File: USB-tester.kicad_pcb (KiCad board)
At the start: 2 copper layers, 68.7 x 41.2 mm, 57 parts

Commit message: Version 2
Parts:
- removed USBC1, USBC2: 105450-0101, USB-C-SMD_TYPE-C-USB-18:USB-C-SMD_TYPE-C-USB-18
- added BAT1: S2B-ZR-SM4A-TF_LF__SN_, S2B-ZR-SM4A-TF_LF__SN_:JST_S2B-ZR-SM4A-TF_LF__SN_, B.Cu at (166.4, 116.1)
- added C1: 10uF, Capacitor_SMD:C_0603_1608Metric, B.Cu at (164.5, 100.5)
- added C2: 10uF, Capacitor_SMD:C_0603_1608Metric, B.Cu at (171.0, 100.4)
- added D1: RED, LED_SMD:LED_0603_1608Metric, F.Cu at (136.1, 110.7)
- added D2: GREEN, LED_SMD:LED_0603_1608Metric, F.Cu at (136.1, 108.9)
- added J1: TYPE-C-31-M-12, TYPE-C-31-M-12:HRO_TYPE-C-31-M-12, B.Cu at (146.9, 121.3)
- added R26: 220R, Resistor_SMD:R_0603_1608Metric, F.Cu at (139.5, 110.7)
- added R27: 5.1K, Resistor_SMD:R_0603_1608Metric, B.Cu at (163.7, 102.8)
- added R28: 220R, Resistor_SMD:R_0603_1608Metric, F.Cu at (139.5, 108.9)
- added R29: 5.1K, Resistor_SMD:R_0603_1608Metric, B.Cu at (153.6, 115.4)
- added R30: 5.1K, Resistor_SMD:R_0603_1608Metric, B.Cu at (153.6, 118.0)
- added U1: TP4057, Package_TO_SOT_SMD:SOT-23-6, B.Cu at (167.7, 100.3)
- added USB1: TYPEC-324-BCP24, easyeda2kicad:USB-C-SMD_TYPEC-324-BCP24, F.Cu at (196.2, 101.5)
- added USB2: TYPEC-324-BCP24, easyeda2kicad:USB-C-SMD_TYPEC-324-BCP24, F.Cu at (136.8, 100.7)
- moved D25 64.3 mm to (198.2, 91.3), turned to 180 degrees
- moved R25 63.4 mm to (198.2, 93.3), turned to 0 degrees
- turned BT2 to 0 degrees
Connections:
- net Net-(A1-K) renamed BAT-
- BT2 pad 1: A10_A -> A10_B
- R1 pad 2: B1_A -> B12_A
- R10 pad 2: B10_A -> B3_A
- R11 pad 2: B11_A -> B2_A
- R12 pad 2: B12_A -> B1_A
- R13 pad 2: A1_B -> A12_A
- R14 pad 2: A2_B -> A11_A
- R15 pad 2: A3_B -> A10_A
- R16 pad 2: A4_B -> A9_A
- R17 pad 2: A5_B -> A8_A
- R18 pad 2: A6_B -> A7_A
- R19 pad 2: A7_B -> A6_A
- R2 pad 2: B2_A -> B11_A
- R20 pad 2: A8_B -> A5_A
- R21 pad 2: A9_B -> A4_A
- R22 pad 2: A10_B -> A3_A
- R23 pad 2: A11_B -> A2_A
- R24 pad 2: A12_B -> A1_A
- R3 pad 2: B3_A -> B10_A
- R4 pad 2: B4_A -> B9_A
- R5 pad 2: B5_A -> B8_A
- R6 pad 2: B6_A -> B7_A
- R7 pad 2: B7_A -> B6_A
- R8 pad 2: B8_A -> B5_A
- R9 pad 2: B9_A -> B4_A
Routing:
- net BAT-: track 96.6 -> 206.7 mm, vias 1 -> 5
- net +5V: track 0.00 -> 63.0 mm, vias 0 -> 4
- net A10_B: track 22.8 -> 85.6 mm, vias 2 -> 3
- net Net-(D2-K): track 0.00 -> 50.2 mm, vias 0 -> 3
- net B5_A: track 15.3 -> 65.2 mm, vias 2 -> 6
- net B11_A: track 17.8 -> 66.6 mm
- net B12_A: track 16.6 -> 64.8 mm, vias 0 -> 1
- net B3_A: track 17.1 -> 65.0 mm
- net B2_A: track 18.6 -> 64.5 mm
- net B10_A: track 19.6 -> 65.1 mm, vias 2 -> 4
- net B1_A: track 17.7 -> 62.1 mm, vias 0 -> 1
- net B8_A: track 22.0 -> 65.4 mm, vias 2 -> 6
- net B4_A: track 14.8 -> 54.3 mm, vias 2 -> 1
- net Net-(D1-K): track 0.00 -> 39.4 mm, vias 0 -> 3
- net B6_A: track 14.4 -> 53.3 mm, vias 2 -> 1
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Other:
- board text added: "+"
- board text added: "-"
- board text added: "CHRG"
- board text added: "STDBY"
- board text added: "USB Tester Version 2.0"
- board text removed: "USB Tester Version 1.0"

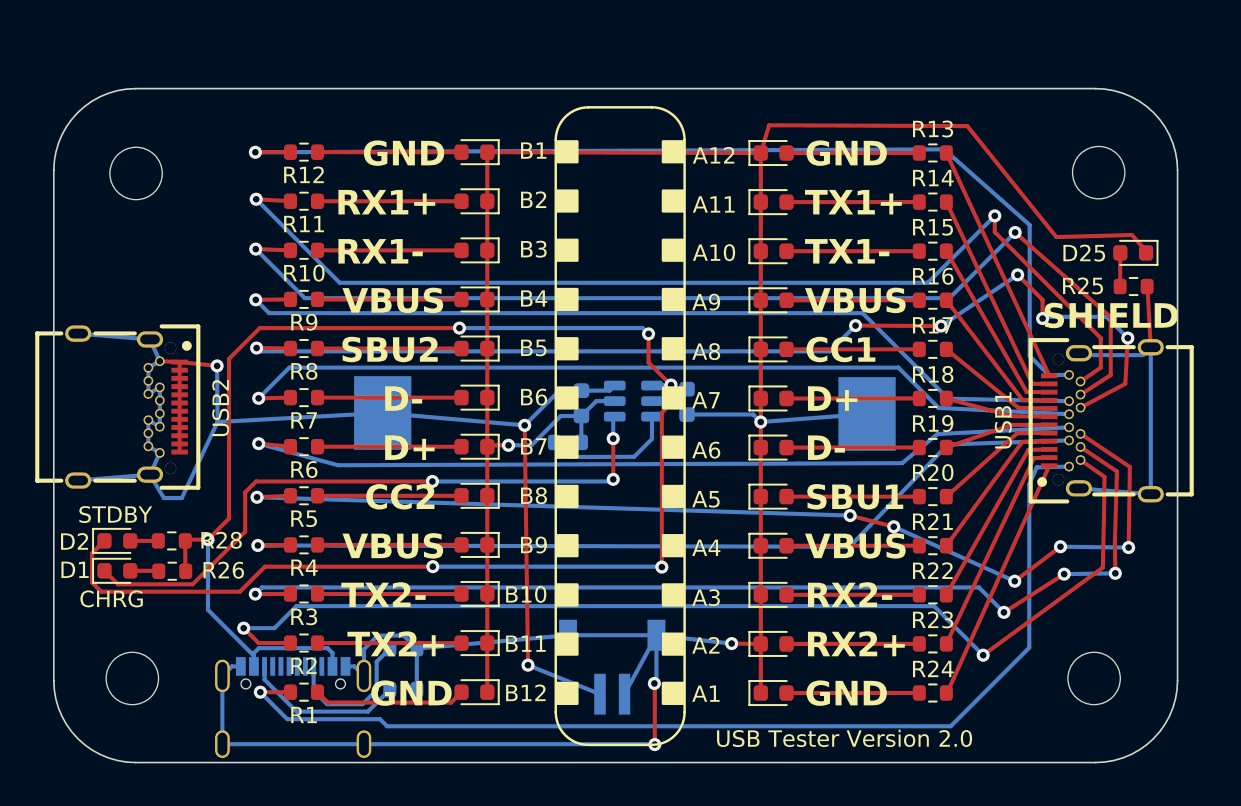
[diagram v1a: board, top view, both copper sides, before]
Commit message: Adds test points
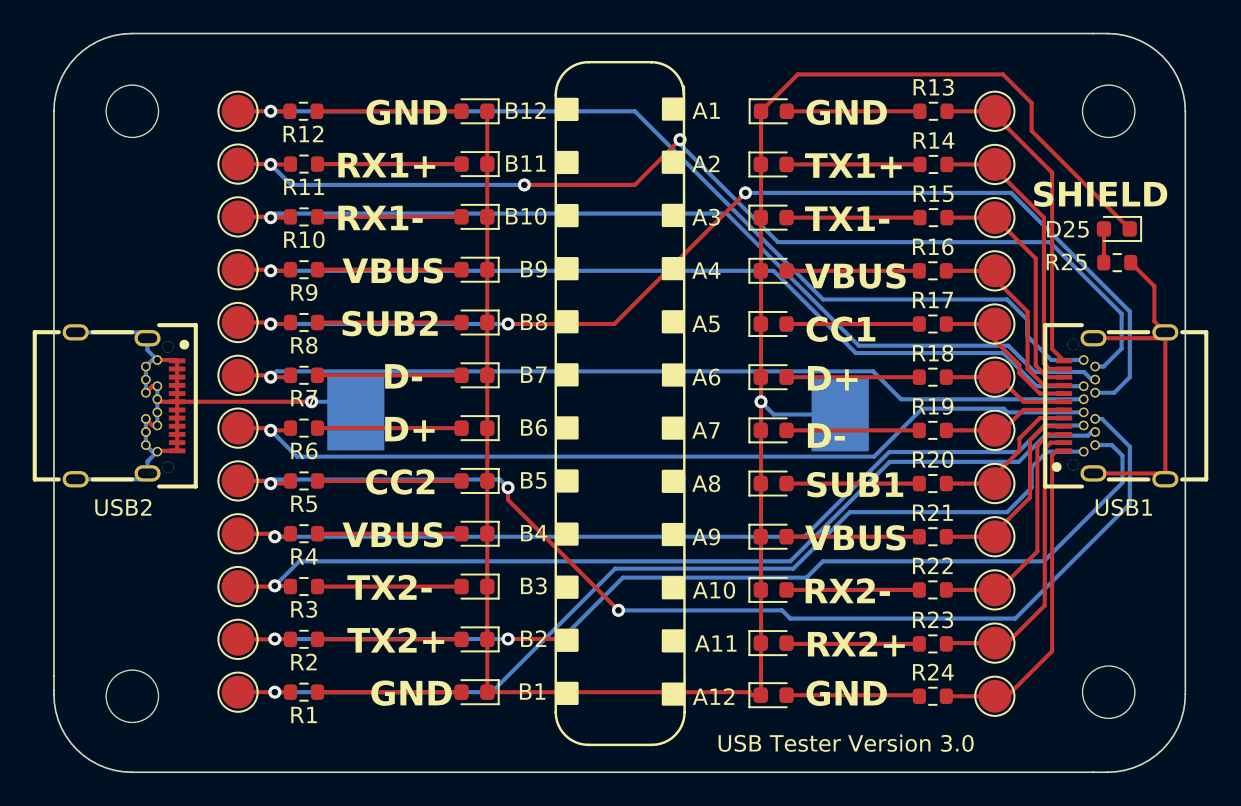
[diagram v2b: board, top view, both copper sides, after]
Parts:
- removed BAT1: S2B-ZR-SM4A-TF_LF__SN_, S2B-ZR-SM4A-TF_LF__SN_:JST_S2B-ZR-SM4A-TF_LF__SN_
- removed C1, C2: 10uF, Capacitor_SMD:C_0603_1608Metric
- removed D1: RED, LED_SMD:LED_0603_1608Metric
- removed D2: GREEN, LED_SMD:LED_0603_1608Metric
- removed J1: TYPE-C-31-M-12, TYPE-C-31-M-12:HRO_TYPE-C-31-M-12
- removed R26, R28: 220R, Resistor_SMD:R_0603_1608Metric
- removed R27, R29, R30: 5.1K, Resistor_SMD:R_0603_1608Metric
- removed U1: TP4057, Package_TO_SOT_SMD:SOT-23-6
- added TP1: GND, TestPoint:TestPoint_Pad_D2.0mm, F.Cu at (189.8, 118.4)
- added TP10: D-, TestPoint:TestPoint_Pad_D2.0mm, F.Cu at (189.8, 98.9)
- added TP11: SUB1, TestPoint:TestPoint_Pad_D2.0mm, F.Cu at (189.8, 95.6)
- added TP12: VBUS, TestPoint:TestPoint_Pad_D2.0mm, F.Cu at (189.8, 92.4)
- added TP13: RX-, TestPoint:TestPoint_Pad_D2.0mm, F.Cu at (189.8, 89.1)
- added TP14: GND, TestPoint:TestPoint_Pad_D2.0mm, F.Cu at (189.8, 82.6)
- added TP15: TX-, TestPoint:TestPoint_Pad_D2.0mm, F.Cu at (143.5, 89.1)
- added TP16: VBUS, TestPoint:TestPoint_Pad_D2.0mm, F.Cu at (143.5, 92.3)
- added TP17: CC2, TestPoint:TestPoint_Pad_D2.0mm, F.Cu at (143.5, 95.5)
- added TP18: D+, TestPoint:TestPoint_Pad_D2.0mm, F.Cu at (143.5, 98.7)
- added TP19: D-, TestPoint:TestPoint_Pad_D2.0mm, F.Cu at (143.5, 102.0)
- added TP2: D+, TestPoint:TestPoint_Pad_D2.0mm, F.Cu at (189.8, 102.1)
- added TP20: SUB2, TestPoint:TestPoint_Pad_D2.0mm, F.Cu at (143.5, 105.2)
- added TP21: VBUS, TestPoint:TestPoint_Pad_D2.0mm, F.Cu at (143.5, 108.4)
- added TP22: RX-, TestPoint:TestPoint_Pad_D2.0mm, F.Cu at (143.5, 111.7)
- added TP23: RX+, TestPoint:TestPoint_Pad_D2.0mm, F.Cu at (143.5, 114.9)
- added TP24: GND, TestPoint:TestPoint_Pad_D2.0mm, F.Cu at (143.5, 118.1)
- added TP3: RX+, TestPoint:TestPoint_Pad_D2.0mm, F.Cu at (189.8, 85.9)
- added TP4: GND, TestPoint:TestPoint_Pad_D2.0mm, F.Cu at (143.5, 82.6)
- added TP5: TX+, TestPoint:TestPoint_Pad_D2.0mm, F.Cu at (143.5, 85.8)
- added TP6: TX+, TestPoint:TestPoint_Pad_D2.0mm, F.Cu at (189.8, 115.1)
- added TP7: TX-, TestPoint:TestPoint_Pad_D2.0mm, F.Cu at (189.8, 111.9)
- added TP8: VBUS, TestPoint:TestPoint_Pad_D2.0mm, F.Cu at (189.8, 108.6)
- added TP9: CC1, TestPoint:TestPoint_Pad_D2.0mm, F.Cu at (189.8, 105.4)
- moved H1 3.81 mm to (137.1, 82.6)
- moved H3 3.80 mm to (196.7, 82.6)
- moved A1 2.55 mm to (176.3, 82.6)
- moved R13 2.55 mm to (186.0, 82.6)
- moved B12 2.50 mm to (158.0, 82.6)
- moved R12 2.50 mm to (147.5, 82.6)
- moved A2 2.30 mm to (176.3, 85.9)
- moved R14 2.30 mm to (186.0, 85.9)
- moved B11 2.27 mm to (158.0, 85.8)
- moved R11 2.27 mm to (147.5, 85.8)
- moved A3 2.05 mm to (176.3, 89.1)
- moved R15 2.05 mm to (186.0, 89.1)
- moved B10 2.05 mm to (158.0, 89.1)
- moved R10 2.04 mm to (147.5, 89.1)
- moved B9 1.82 mm to (158.0, 92.3)
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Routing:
- net BAT-: track 206.7 -> 121.5 mm, vias 5 -> 1
- net +5V: track 63.0 -> 0.00 mm, vias 4 -> 0
- net Net-(D2-K): track 50.2 -> 0.00 mm, vias 3 -> 0
- net A10_B: track 85.6 -> 41.7 mm, vias 3 -> 1
- net Net-(D1-K): track 39.4 -> 0.00 mm, vias 3 -> 0
- net Net-(J1-CC2): track 9.83 -> 0.00 mm
- net Net-(J1-CC1): track 8.90 -> 0.00 mm
- net Net-(U1-PROG): track 8.15 -> 0.00 mm
- net B10_A: track 65.1 -> 57.3 mm, vias 4 -> 1
- net B3_A: track 65.0 -> 58.0 mm, vias 2 -> 1
- net B8_A: track 65.4 -> 71.2 mm, vias 6 -> 3
- net B12_A: track 64.8 -> 59.5 mm
- net A12_A: track 15.0 -> 19.8 mm
- net A1_A: track 15.2 -> 20.0 mm
- net A2_A: track 13.5 -> 17.9 mm
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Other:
- board size 68.7 x 41.2 mm -> 69.1 x 45.1 mm
- board text added: "SUB1"
- board text added: "SUB2"
- board text added: "USB Tester Version 3.0"
- board text removed: "CHRG"
- board text removed: "SBU1"
- board text removed: "SBU2"
- board text removed: "STDBY"
- board text removed: "USB Tester Version 2.0"

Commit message: Break out version
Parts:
- removed TP1, TP14, TP24, TP4: GND, TestPoint:TestPoint_Pad_D2.0mm
- removed TP10, TP19: D-, TestPoint:TestPoint_Pad_D2.0mm
- removed TP11: SUB1, TestPoint:TestPoint_Pad_D2.0mm
- removed TP12, TP16, TP21, TP8: VBUS, TestPoint:TestPoint_Pad_D2.0mm
- removed TP13, TP22: RX-, TestPoint:TestPoint_Pad_D2.0mm
- removed TP15, TP7: TX-, TestPoint:TestPoint_Pad_D2.0mm
- removed TP17: CC2, TestPoint:TestPoint_Pad_D2.0mm
- removed TP18, TP2: D+, TestPoint:TestPoint_Pad_D2.0mm
- removed TP20: SUB2, TestPoint:TestPoint_Pad_D2.0mm
- removed TP23, TP3: RX+, TestPoint:TestPoint_Pad_D2.0mm
- removed TP5, TP6: TX+, TestPoint:TestPoint_Pad_D2.0mm
- removed TP9: CC1, TestPoint:TestPoint_Pad_D2.0mm
- added J1: Conn_02x12_Odd_Even, Connector_PinSocket_2.54mm:PinSocket_2x12_P2.54mm_Vertical, F.Cu at (165.5, 114.2)
- added J2: Conn_01x02, Connector_PinSocket_2.54mm:PinSocket_1x02_P2.54mm_Vertical, F.Cu at (136.5, 92.1)
- moved BT2 14.5 mm to (151.0, 100.1), turned to 90 degrees
- moved R24 4.04 mm to (186.0, 114.3)
- moved A12 3.93 mm to (176.3, 114.4)
- moved R1 3.79 mm to (147.5, 114.3)
- moved B1 3.75 mm to (158.0, 114.4)
- moved B12 3.54 mm to (158.0, 86.1)
- moved A1 3.54 mm to (176.3, 86.1)
- moved R12 3.50 mm to (147.5, 86.1)
- moved R13 3.50 mm to (186.0, 86.1)
- moved R23 3.40 mm to (186.0, 111.8)
- moved A11 3.32 mm to (176.3, 111.8)
- moved R2 3.13 mm to (147.5, 111.8)
- moved B2 3.09 mm to (158.0, 111.8)
- moved B11 2.84 mm to (158.0, 88.7)
- moved R11 2.84 mm to (147.5, 88.7)
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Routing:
- net BAT-: track 121.5 -> 157.7 mm, vias 1 -> 25
- net A10_B: track 41.7 -> 72.3 mm
- net A7_A: track 7.80 -> 27.2 mm
- net A6_A: track 7.70 -> 26.9 mm
- net A8_A: track 9.24 -> 28.1 mm
- net A5_A: track 9.28 -> 27.8 mm
- net A3_A: track 14.9 -> 32.0 mm
- net A9_A: track 12.1 -> 28.9 mm
- net A4_A: track 12.0 -> 28.8 mm
- net A2_A: track 17.9 -> 33.9 mm
- net A10_A: track 15.0 -> 30.6 mm
- net A1_A: track 20.0 -> 35.2 mm
- net A11_A: track 17.5 -> 32.5 mm
- net A12_A: track 19.8 -> 34.2 mm
- net B8_A: track 71.2 -> 58.1 mm
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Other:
- board size 69.1 x 45.1 mm -> 69.1 x 41 mm
- board text added: "USB1"

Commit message: Adds images and README file
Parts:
- A1, A12, B1, B12: value LED -> LEDW
- A10, A11, A2, A3, B10, B11, B2, B3: value LED -> LEDY
- A4, A9, B4, B9: value LED -> LEDR
- A5, B5: value LED -> LEDB
- A6, A7, B6, B7: value LED -> LEDG
- A8, B8: value LED -> LEDV
- R1, R10, R11, R12, R13, R14, R15, R16, R17, R18, R19, R2, R20, R21, R22, R23, R24, R3, R4, R5, R6, R7, R8, R9: value 1000 -> 100
